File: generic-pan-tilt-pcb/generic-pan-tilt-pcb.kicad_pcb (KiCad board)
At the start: 2 copper layers, 104 x 57 mm, 90 parts, among them J1 B4P-VH-FB-B, J10 USB4105-GF-A, J11 Conn_01x08, J12 Conn_01x08, J13 Conn_01x05, J2 NC5MAV, J3 NC5FAV, J5 BM03B-SRSS-TBT, J7 BM03B-SRSS-TBT, J8 B12B-PH-SM4-TBT, J9 B12B-PH-SM4-TBT, SW1 PTS 647 SK70 SMTR2 LFS, SW2 PTS 647 SK70 SMTR2 LFS, SW3 219-12LPST, U1 RP2040, U2 W25Q128JVS, U3 AP63203WU, U4 ISO1450DW, U5 MCP23017_SO, U6 LIS3DH, Y1 ABM8-272-T3

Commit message: fix overlap in kibot vars
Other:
- board text added: "Rev: ${KIBOT_GIT_DESCRIBE} ${KIBOT_GIT_DATE} ${KITBOT_RUN_DATE}"
- board text removed: "${KIBOT_GIT_DESCRIBE} ${KIBOT_GIT_DATE} ${KITBOT_RUN_DATE}"
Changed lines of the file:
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@@
 		)
 	)
-	(gr_text "${KIBOT_GIT_DESCRIBE}\n${KIBOT_GIT_DATE}\n${KITBOT_RUN_DATE}"
+	(gr_text "Rev: ${KIBOT_GIT_DESCRIBE}\n${KIBOT_GIT_DATE}\n${KITBOT_RUN_DATE}"
 		(at 167.45 119.95 0)
 		(layer "B.SilkS")

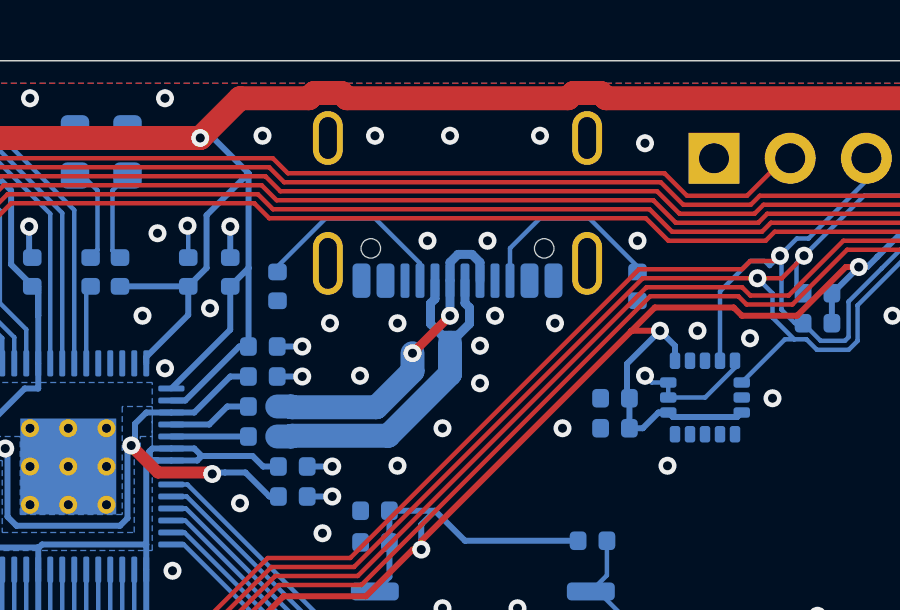
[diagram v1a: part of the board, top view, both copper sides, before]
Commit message: fix usb drc errors
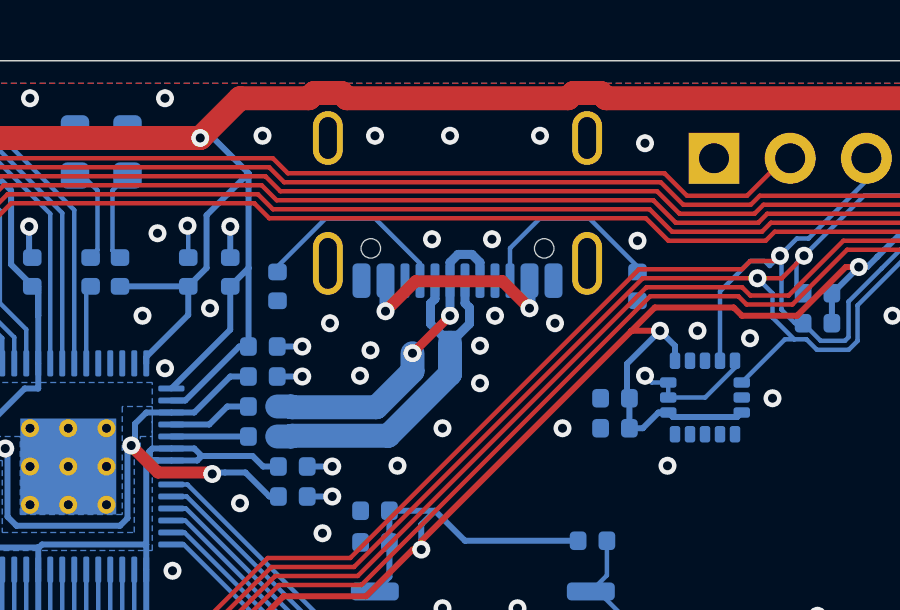
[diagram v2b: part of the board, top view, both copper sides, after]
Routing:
- net VBUS: track 0.00 -> 7.53 mm, vias 0 -> 2

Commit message: fix LED resistors
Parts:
- L1: value VLS6045EX-6R8M -> 6.8µH 3.6A 36MΩ
- L2: value 82103C -> 10µH 500mA 400MΩ
- R18: value 108Ω -> 65Ω
- R19: value 17Ω -> 65Ω
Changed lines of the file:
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@@
 			)
 		)
-		(property "Value" "108Ω"
+		(property "Value" "65Ω"
 			(at 0 -1.16 90)
 			(layer "B.Fab")
@@
 			)
 		)
-		(property "Value" "17Ω"
+		(property "Value" "65Ω"
 			(at 0 -1.16 90)
 			(layer "B.Fab")
@@
 			)
 		)
-		(property "Value" "82103C"
+		(property "Value" "10µH 500mA 400MΩ"
 			(at 0 -2.28 90)
 			(layer "B.Fab")
@@
 			)
 		)
-		(property "Value" "VLS6045EX-6R8M"
+		(property "Value" "6.8µH 3.6A 36MΩ"
 			(at 0 -4 0)
 			(unlocked yes)

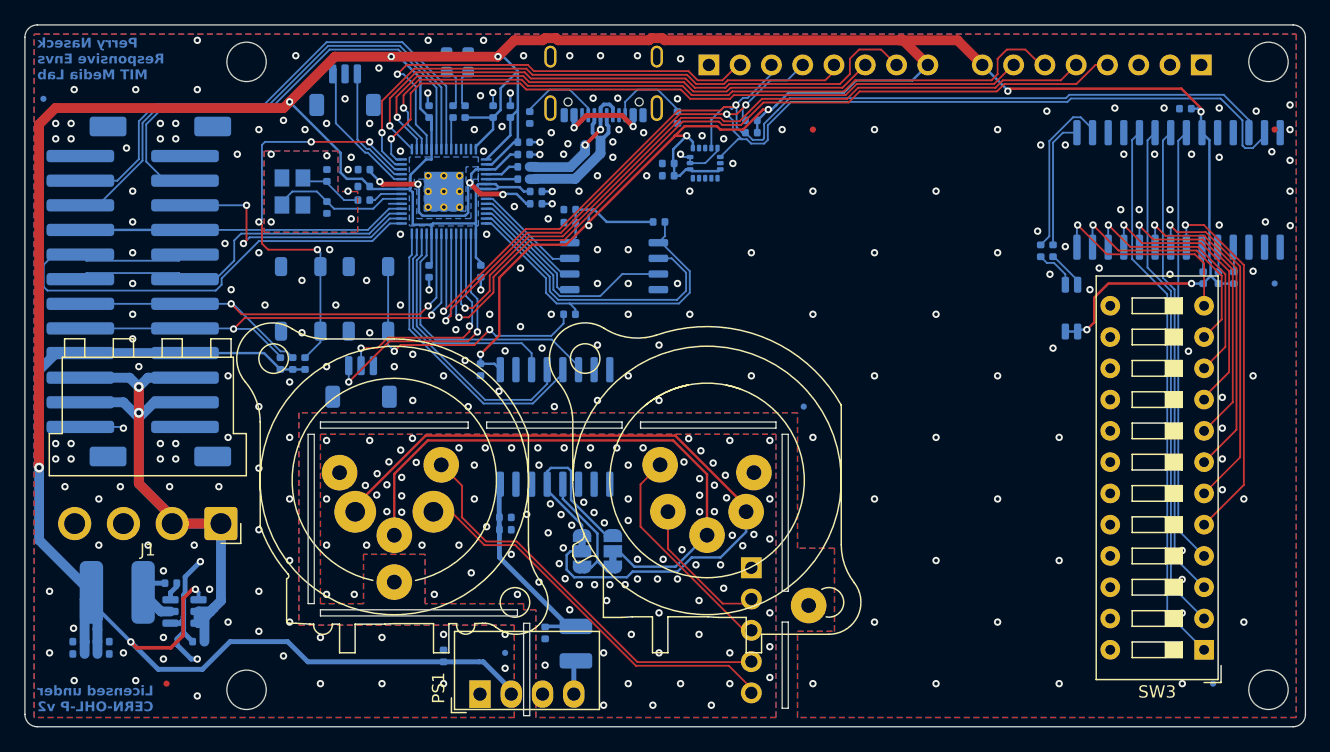
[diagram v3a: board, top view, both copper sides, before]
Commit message: fix c footprint for r
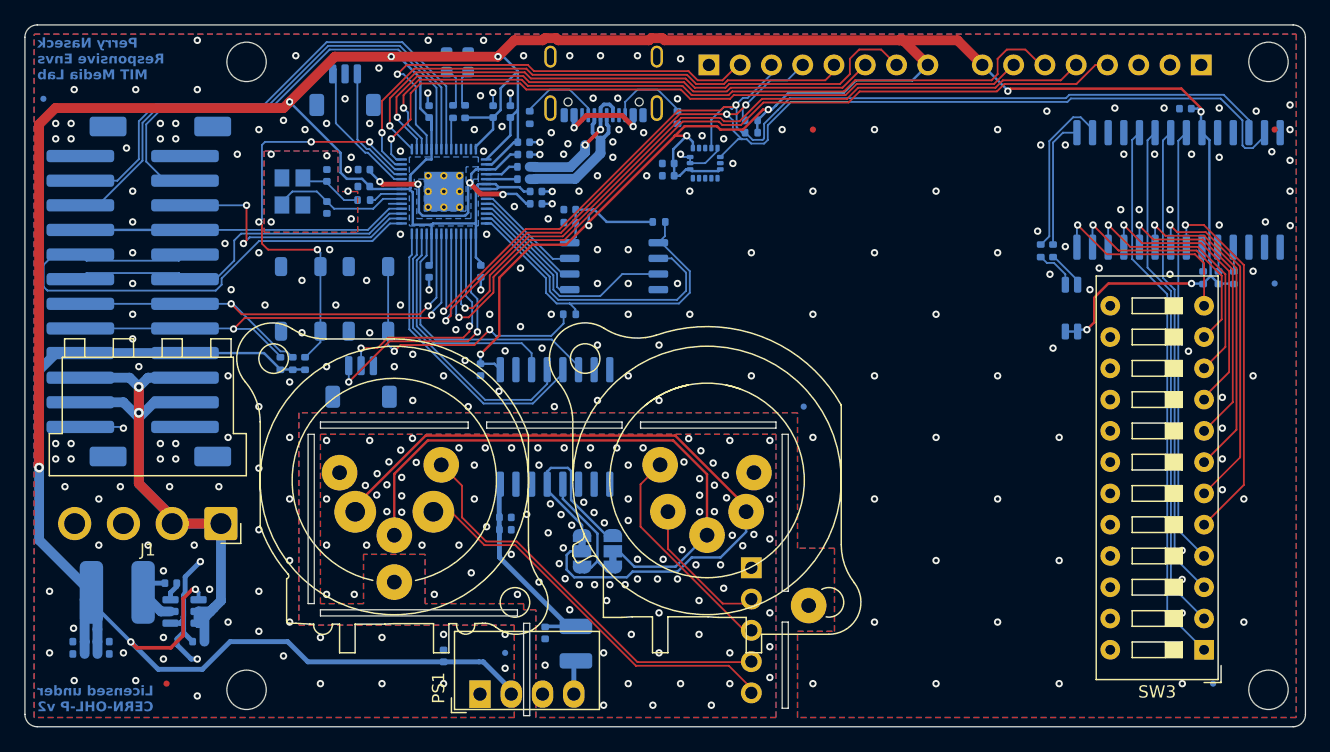
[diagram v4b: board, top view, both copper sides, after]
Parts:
- R1, R10, R11, R12, R13, R14, R15, R16, R17, R18, R19, R2, R3, R4, R5, R6, R7, R8, R9: footprint Capacitor_SMD:C_0402_1005Metric -> Resistor_SMD:R_0402_1005Metric

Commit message: 0603 caps for psu rs485
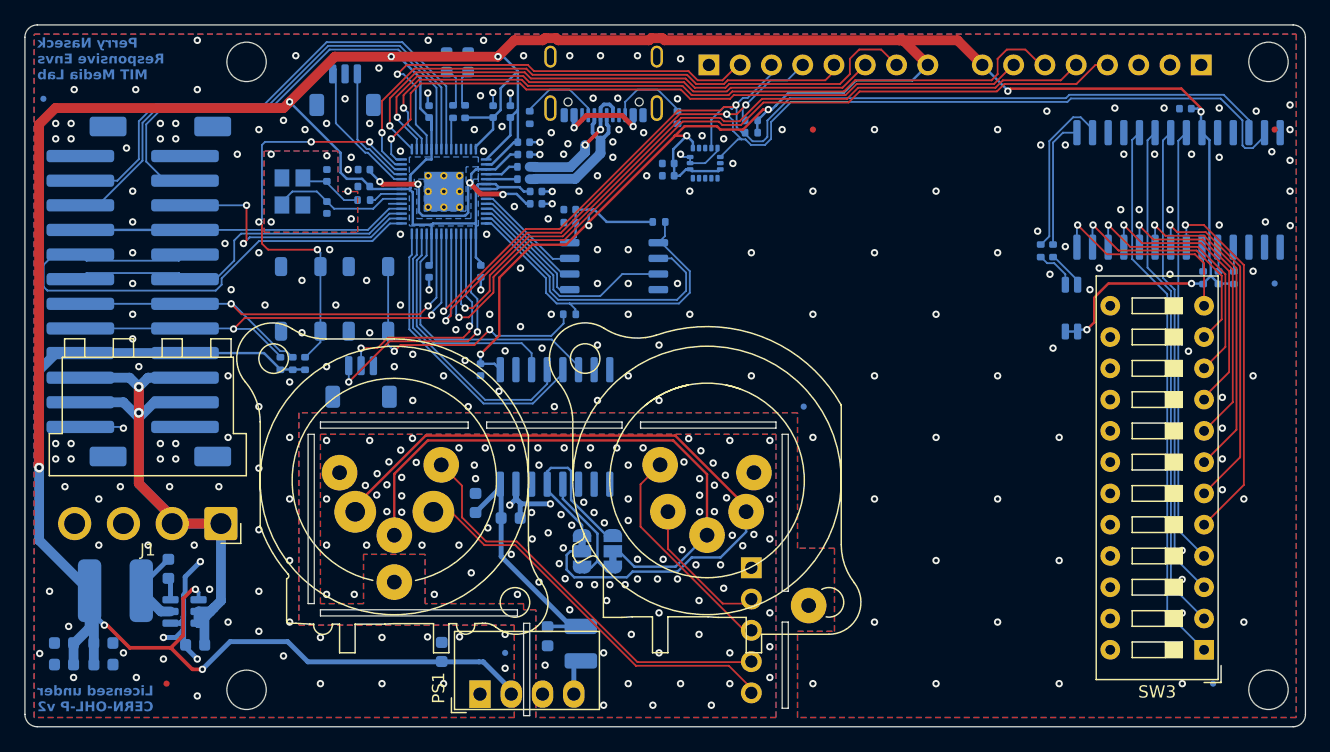
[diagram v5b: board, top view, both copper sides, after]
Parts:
- C17, C18, C19, C20, C21, C22, C23, C25, C26, C27: footprint Capacitor_SMD:C_0402_1005Metric -> Capacitor_SMD:C_0603_1608Metric
- moved C27 3.25 mm to (117.6, 105.3), turned to 90 degrees
- moved C22 1.47 mm to (84.2, 118.5)
- moved C21 1.20 mm to (84.2, 116.7)
- moved C18 1.18 mm to (92.7, 110.7), turned to 90 degrees
- moved C20 0.86 mm to (87.4, 118.5)
- moved C25 0.43 mm to (120.5, 106.5)
- moved L2 0.40 mm to (126.2, 116.8)
- moved C17 0.38 mm to (94.8, 116.8)
- moved C23 0.36 mm to (114.8, 117.4)
- moved C26 0.34 mm to (123.5, 116.2)
- moved L1 0.20 mm to (88.3, 112.5)
- moved C19 0.11 mm to (87.4, 116.7)
- renumbered FID6 to FID4, FID4 to FID5, FID7 to FID6, FID5 to FID7, R9 to R8, R8 to R9
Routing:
- net /RS485_GND: track 0.06 -> 7.83 mm, vias 103 -> 105
- net /generic-pan-tilt-pcb_rs485/+3V3_ISO: track 16.9 -> 20.8 mm
- net /generic-pan-tilt-pcb_24v_to_3.3v/+3V3_UNFILTERED: track 5.01 -> 6.84 mm
- net GND: track 30.0 -> 30.9 mm
- net +3V3: track 423.3 -> 424.1 mm, vias 14 -> 15
